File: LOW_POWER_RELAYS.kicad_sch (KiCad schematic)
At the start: 8 parts, among them CN1 6437288-3, U1 YQ506-S-112 DM

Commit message: Modified Relay Page to add Lights, Radiator, and Fuel Pump
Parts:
- removed D2: LED, symbol Device:LED
- removed R1: 10k, symbol Device:R_US
- removed R2: ?, symbol Device:R_US
- added C10: 100n, EasyEDA:CAP-TH_L5.0-W2.5-P5.00-D1.0, symbol Device:C
- added C11, C12, C9: 10u, EasyEDA:CAP-TH_L5.5-W3.8-P5.08-D0.5, symbol Device:C
- added D3, D5: 1N5399, Package_DIP:DIP-40_W15.24mm, symbol Device:D_Zener
- added D6, D7, D8: LED, EasyEDA:LED-TH_BD3.0-P2.54-FD_YELLOW, symbol Device:LED
- added R10, R6, R9: 660, EasyEDA:RES-TH_BD2.4-L6.3-P10.30-D0.6, symbol Device:R_US
- added R5, R7, R8: 10k, EasyEDA:RES-TH_BD2.5-L6.5-P10.50-D0.6, symbol Device:R_US
- added U2, U3: YQ506-S-112 DM, EasyEDA:RELAY-TH_YQ506-S-112DM, symbol EasyEDA:YQ506-S-112DM
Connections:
- net GND: now also C10.2, C11.2, C12.2, C9.2, D3.2 (A), D5.2 (A), R10.2, R5.2, R6.2, R7.2, R8.2, R9.2, U2.86, U3.86
- net PWR_12V: now also C10.1, C11.1, C12.1, C9.1, U2.30, U3.30
- net PWR_EN_FUEL_PUMP: now also D7.2 (A), R7.1
- new net: D8.1 (K), R9.1
- new net: D6.1 (K), R6.1
- new net: D7.1 (K), R10.1
- new net PWR_EN_LIGHTS: D3.1 (K), D8.2 (A), R8.1, U2.85
- new net PWR_EN_RADIATOR: D5.1 (K), D6.2 (A), R5.1, U3.85
- new net PWR_LIGHTS: U2.87
- new net PWR_RADIATOR: U3.87
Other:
- note added: "Author: Brandon Estrada"
- note removed: "We need: 3x THT LEDs, various colors, with THT resistors 1x THT Buzzer, 5V rated"
- moved on the sheet: C7, C8, D1, U1

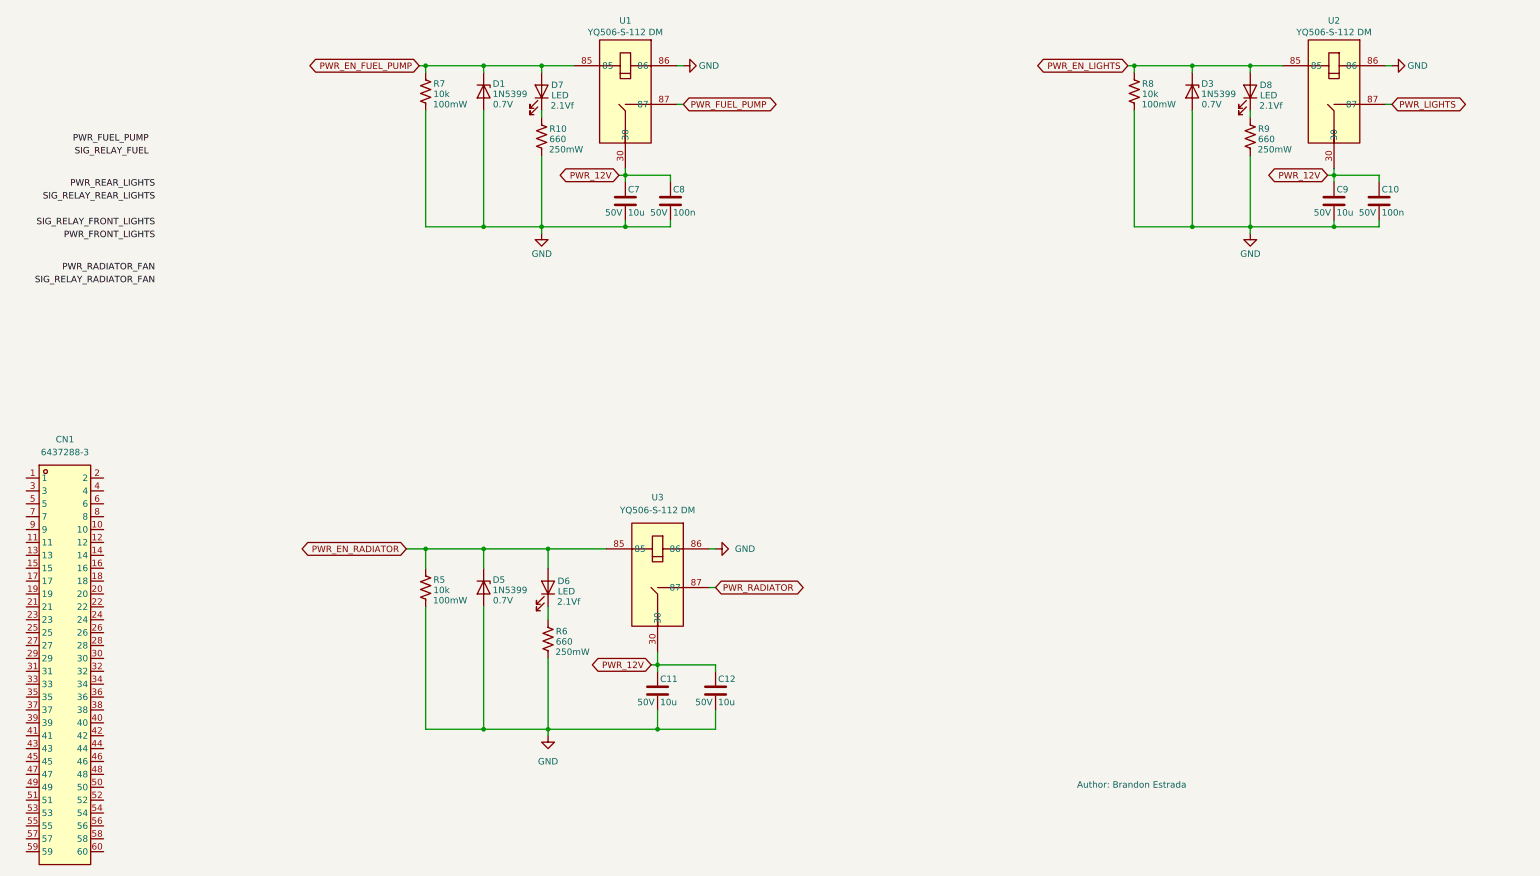
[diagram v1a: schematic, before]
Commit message: Update hub design and add RJ45 connector
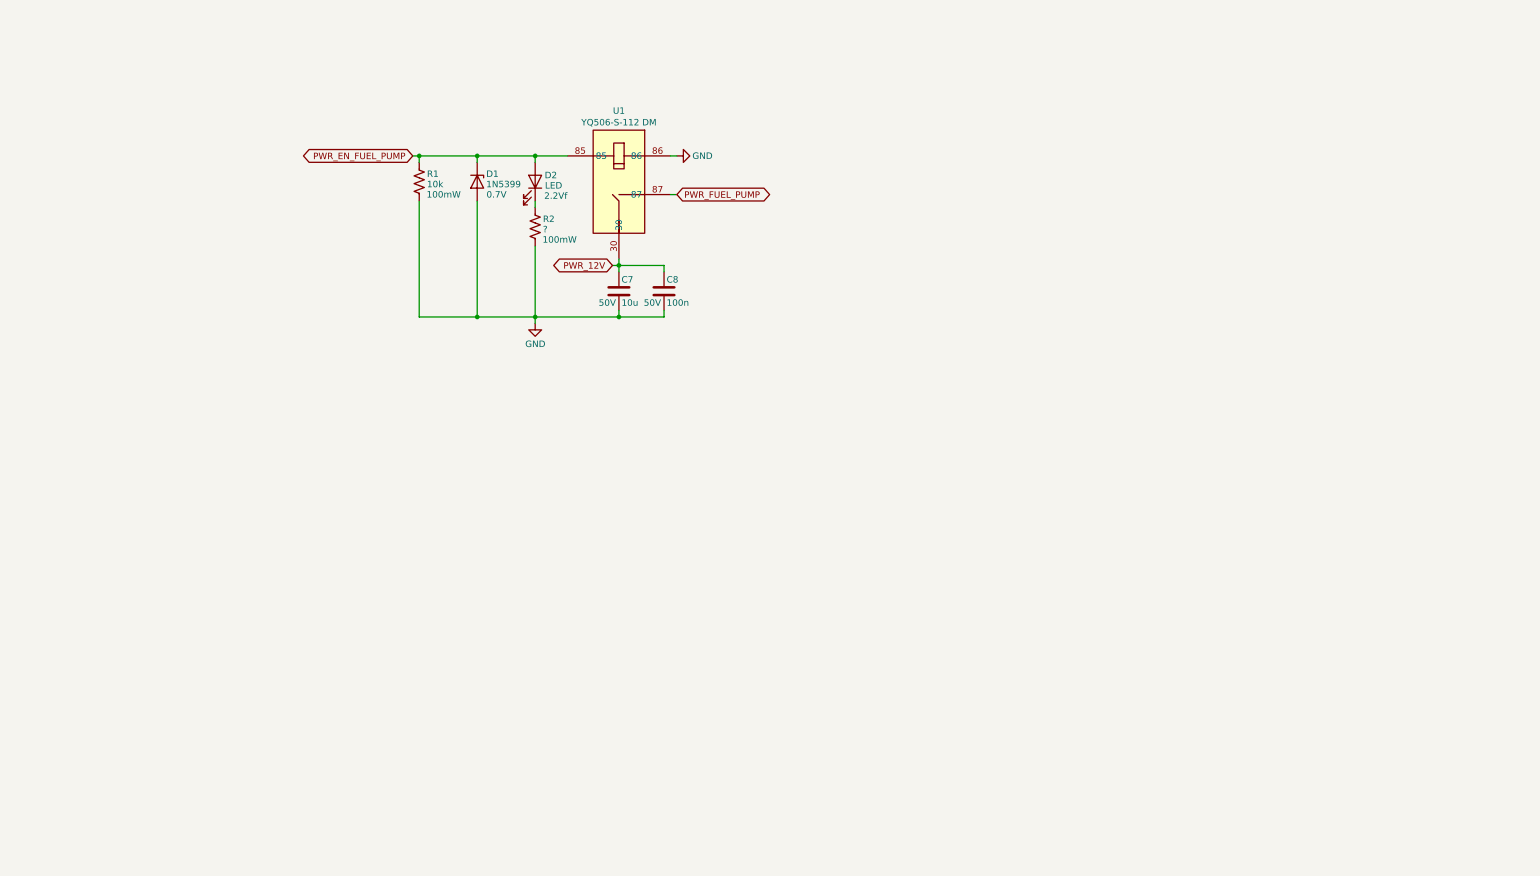
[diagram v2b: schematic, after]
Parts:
- removed C10: 100n, EasyEDA:CAP-TH_L5.0-W2.5-P5.00-D1.0, symbol Device:C
- removed C11, C12, C9: 10u, EasyEDA:CAP-TH_L5.5-W3.8-P5.08-D0.5, symbol Device:C
- removed CN1: 6437288-3, EasyEDA:DSUB-60P_SUPERSEAL, symbol EasyEDA:6437288-3
- removed D3, D5: 1N5399, Package_DIP:DIP-40_W15.24mm, symbol Device:D_Zener
- removed D6, D7, D8: LED, EasyEDA:LED-TH_BD3.0-P2.54-FD_YELLOW, symbol Device:LED
- removed R10, R6, R9: 660, EasyEDA:RES-TH_BD2.4-L6.3-P10.30-D0.6, symbol Device:R_US
- removed R5, R7, R8: 10k, EasyEDA:RES-TH_BD2.5-L6.5-P10.50-D0.6, symbol Device:R_US
- removed U2, U3: YQ506-S-112 DM, EasyEDA:RELAY-TH_YQ506-S-112DM, symbol EasyEDA:YQ506-S-112DM
- added D2: LED, symbol Device:LED
- added R1: 10k, symbol Device:R_US
- added R2: ?, symbol Device:R_US
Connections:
- net GND: now also R1.2, R2.2
- net PWR_EN_FUEL_PUMP: now also D2.2 (A), R1.1
- new net: D2.1 (K), R2.1
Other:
- note removed: "Author: Brandon Estrada"
- moved on the sheet: C7, C8, D1, U1

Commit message: Merge relay and status schematic components
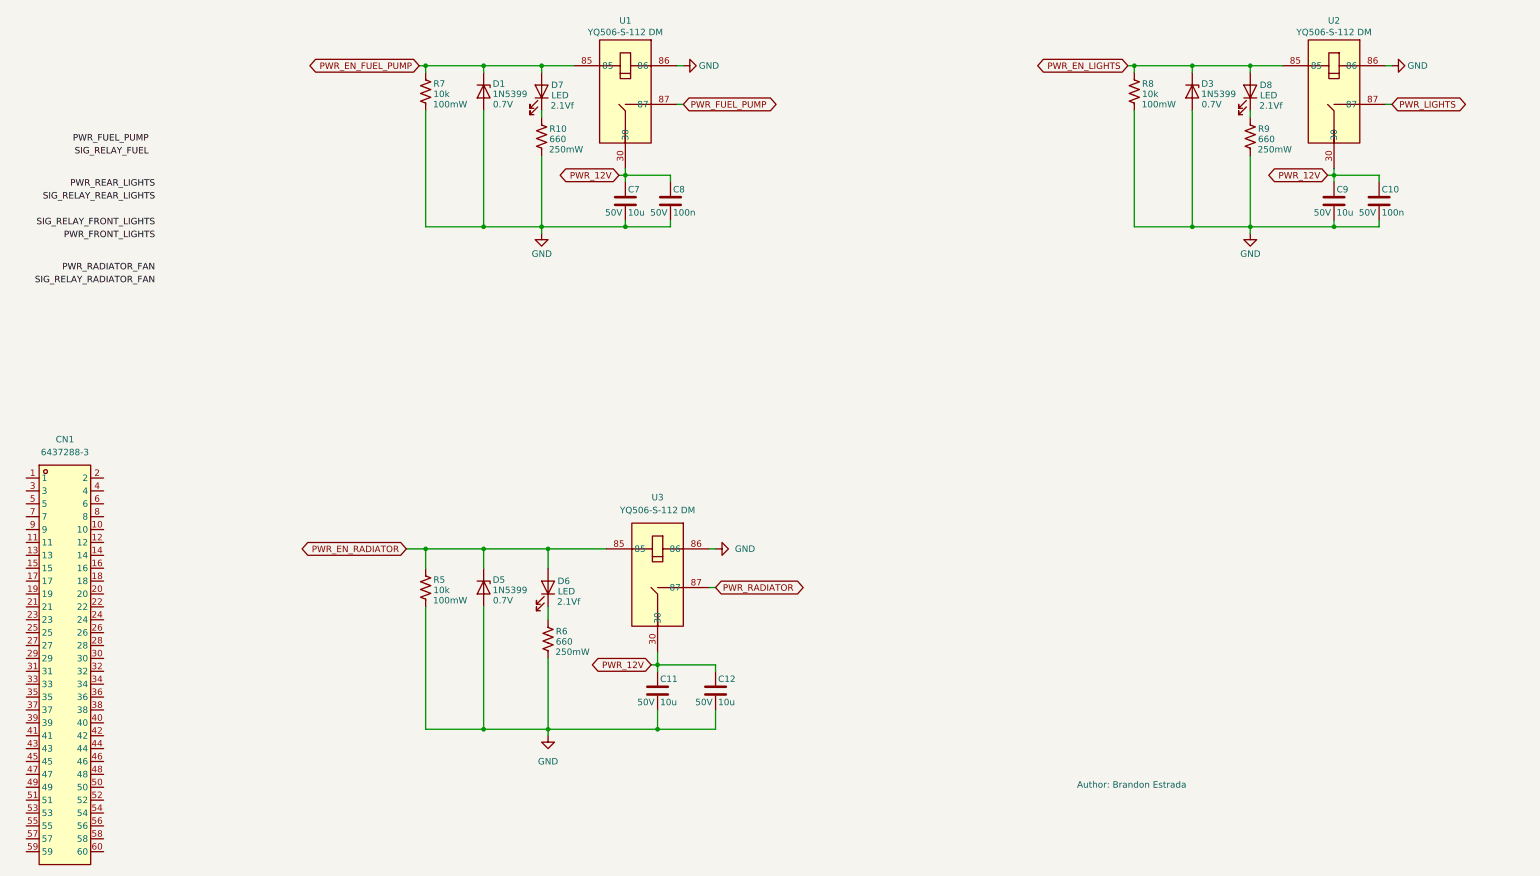
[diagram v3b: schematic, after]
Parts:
- removed D2: LED, symbol Device:LED
- removed R1: 10k, symbol Device:R_US
- removed R2: ?, symbol Device:R_US
- added C10: 100n, EasyEDA:CAP-TH_L5.0-W2.5-P5.00-D1.0, symbol Device:C
- added C11, C12, C9: 10u, EasyEDA:CAP-TH_L5.5-W3.8-P5.08-D0.5, symbol Device:C
- added CN1: 6437288-3, EasyEDA:DSUB-60P_SUPERSEAL, symbol EasyEDA:6437288-3
- added D3, D5: 1N5399, Package_DIP:DIP-40_W15.24mm, symbol Device:D_Zener
- added D6, D7, D8: LED, EasyEDA:LED-TH_BD3.0-P2.54-FD_YELLOW, symbol Device:LED
- added R10, R6, R9: 660, EasyEDA:RES-TH_BD2.4-L6.3-P10.30-D0.6, symbol Device:R_US
- added R5, R7, R8: 10k, EasyEDA:RES-TH_BD2.5-L6.5-P10.50-D0.6, symbol Device:R_US
- added U2, U3: YQ506-S-112 DM, EasyEDA:RELAY-TH_YQ506-S-112DM, symbol EasyEDA:YQ506-S-112DM
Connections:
- net GND: now also C10.2, C11.2, C12.2, C9.2, D3.2 (A), D5.2 (A), R10.2, R5.2, R6.2, R7.2, R8.2, R9.2, U2.86, U3.86
- net PWR_12V: now also C10.1, C11.1, C12.1, C9.1, U2.30, U3.30
- net PWR_EN_FUEL_PUMP: now also D7.2 (A), R7.1
- new net: D8.1 (K), R9.1
- new net: D6.1 (K), R6.1
- new net: D7.1 (K), R10.1
- new net PWR_EN_LIGHTS: D3.1 (K), D8.2 (A), R8.1, U2.85
- new net PWR_EN_RADIATOR: D5.1 (K), D6.2 (A), R5.1, U3.85
- new net PWR_LIGHTS: U2.87
- new net PWR_RADIATOR: U3.87
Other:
- note added: "Author: Brandon Estrada"
- moved on the sheet: C7, C8, D1, U1

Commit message: Cleanup schematics a little bit
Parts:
- removed CN1: 6437288-3, EasyEDA:DSUB-60P_SUPERSEAL, symbol EasyEDA:6437288-3
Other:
- note added: "0"
- note added: "Authors: Isaac Subudhi Brandon Estrada"
- note added: "Mon, Oct, 12, 2026"
- note added: "RAM RACING: HUB V2: Low Power Relays"
- note removed: "Author: Brandon Estrada"
- moved on the sheet: C10, C11, C12, C9, D3, D5, D6, D8, R5, R6, R8, R9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

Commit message: Mapping for M130, cleanup on all sheets, layout start
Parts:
- added C10: 10u, EasyEDA:CAP-TH_L5.5-W3.8-P5.08-D0.5, symbol Device:C
- added C13: 100n, EasyEDA:CAP-TH_L5.0-W2.5-P5.00-D1.0, symbol Device:C
- added D6: 1N5399, Diode_THT:D_DO-15_P10.16mm_Horizontal, symbol Device:D_Zener
- added D9: LED, EasyEDA:LED-TH_BD3.0-P2.54-FD_YELLOW, symbol Device:LED
- added R6: 10k, EasyEDA:RES-TH_BD2.5-L6.5-P10.50-D0.6, symbol Device:R_US
- added R9: 660, EasyEDA:RES-TH_BD2.4-L6.3-P10.30-D0.6, symbol Device:R_US
- added U3: YQ506-S-112 DM, EasyEDA:RELAY-TH_YQ506-S-112DM, symbol EasyEDA:YQ506-S-112DM
- C12: value 10u -> 100n; footprint EasyEDA:CAP-TH_L5.5-W3.8-P5.08-D0.5 -> EasyEDA:CAP-TH_L5.0-W2.5-P5.00-D1.0; LCSC Num (none) -> C254085; LCSC Part C2761740 -> (none)
- D10: renamed from D3; footprint Package_DIP:DIP-40_W15.24mm -> Diode_THT:D_DO-15_P10.16mm_Horizontal
- D4: renamed from D5; footprint Package_DIP:DIP-40_W15.24mm -> Diode_THT:D_DO-15_P10.16mm_Horizontal
- D5: renamed from D1; footprint Package_DIP:DIP-40_W15.24mm -> Diode_THT:D_DO-15_P10.16mm_Horizontal
- renumbered C8 to C11, C9 to C14, C10 to C15, C7 to C8, C11 to C9, D8 to D11, D6 to D7, D7 to D8, R8 to R10, R9 to R11, R5 to R4, R7 to R5, R6 to R7, R10 to R8, U3 to U2, U2 to U4
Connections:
- net GND: now also C10.2, C13.2, D6.2 (A), R6.2, R9.2, U3.86
- net PWR_12V renamed +12V_BATT
- net +12V_BATT: now also C10.1, C13.1, U3.30
- net PWR_EN_FUEL_PUMP renamed EN_HS_FUEL_PUMP
- net PWR_EN_LIGHTS renamed EN_HS_LIGHTS
- net PWR_EN_RADIATOR renamed EN_HS_RADIATOR
- new net: D9.1 (K), R9.1
- new net +12V_MAIN: U3.87
- new net PWR_EN_MAIN: D6.1 (K), D9.2 (A), R6.1, U3.85
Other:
- note added: "Authors: Lead: Isaac Subudhi Main Editor: Brandon Estrada"
- note removed: "Authors: Isaac Subudhi Brandon Estrada"
- moved on the sheet: C11, C14, C15, C8, C9, D10, D11, D4, D5, D7, D8, R10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

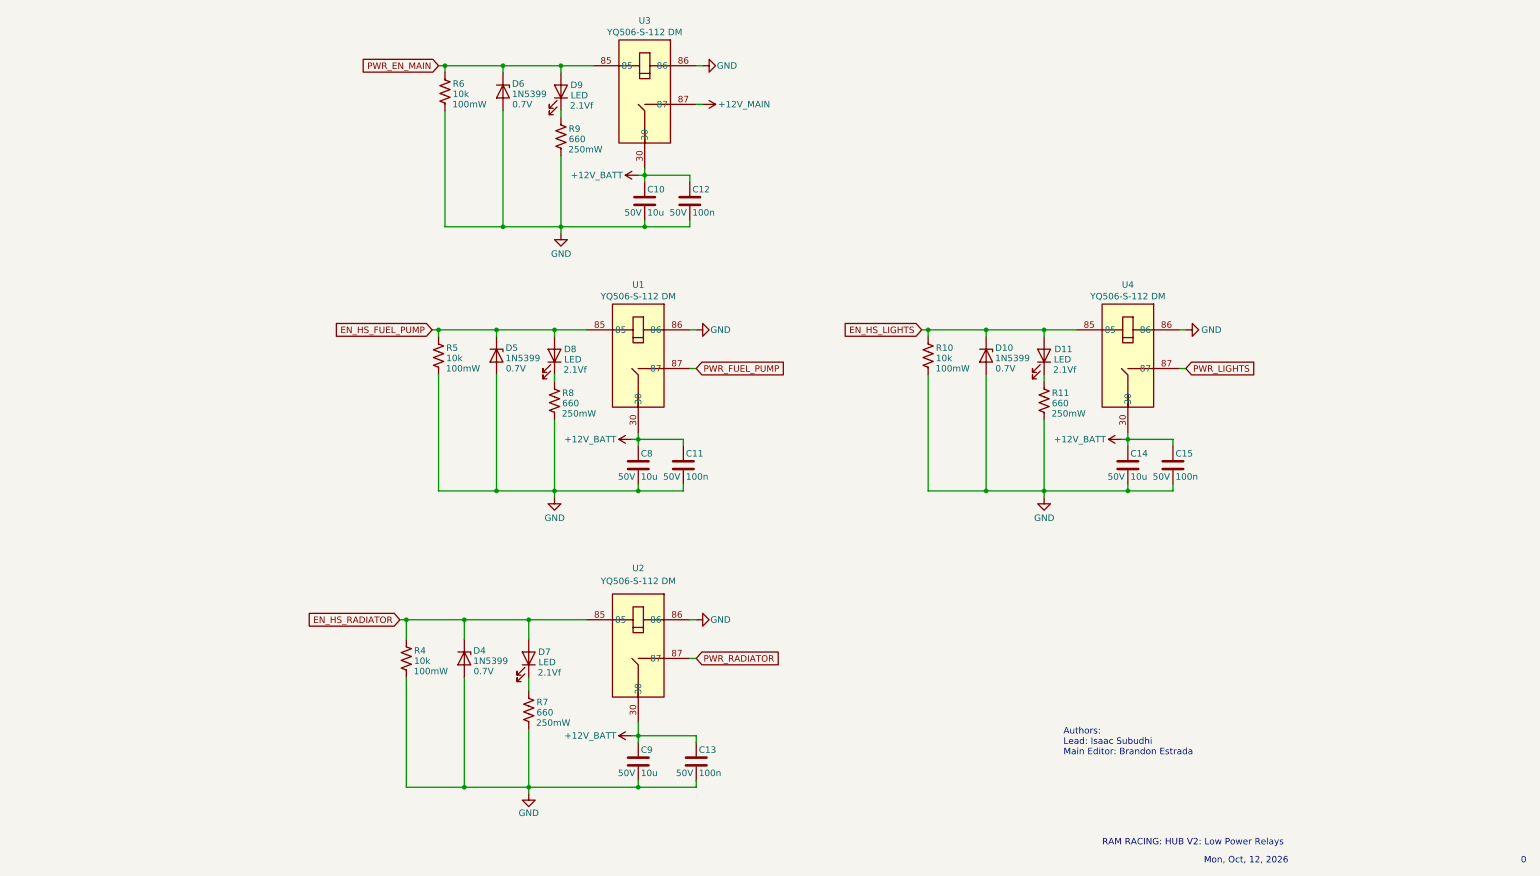
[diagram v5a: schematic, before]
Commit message: Relay layout done, pinout assignments, M1 Notes, and 04 Sch Start
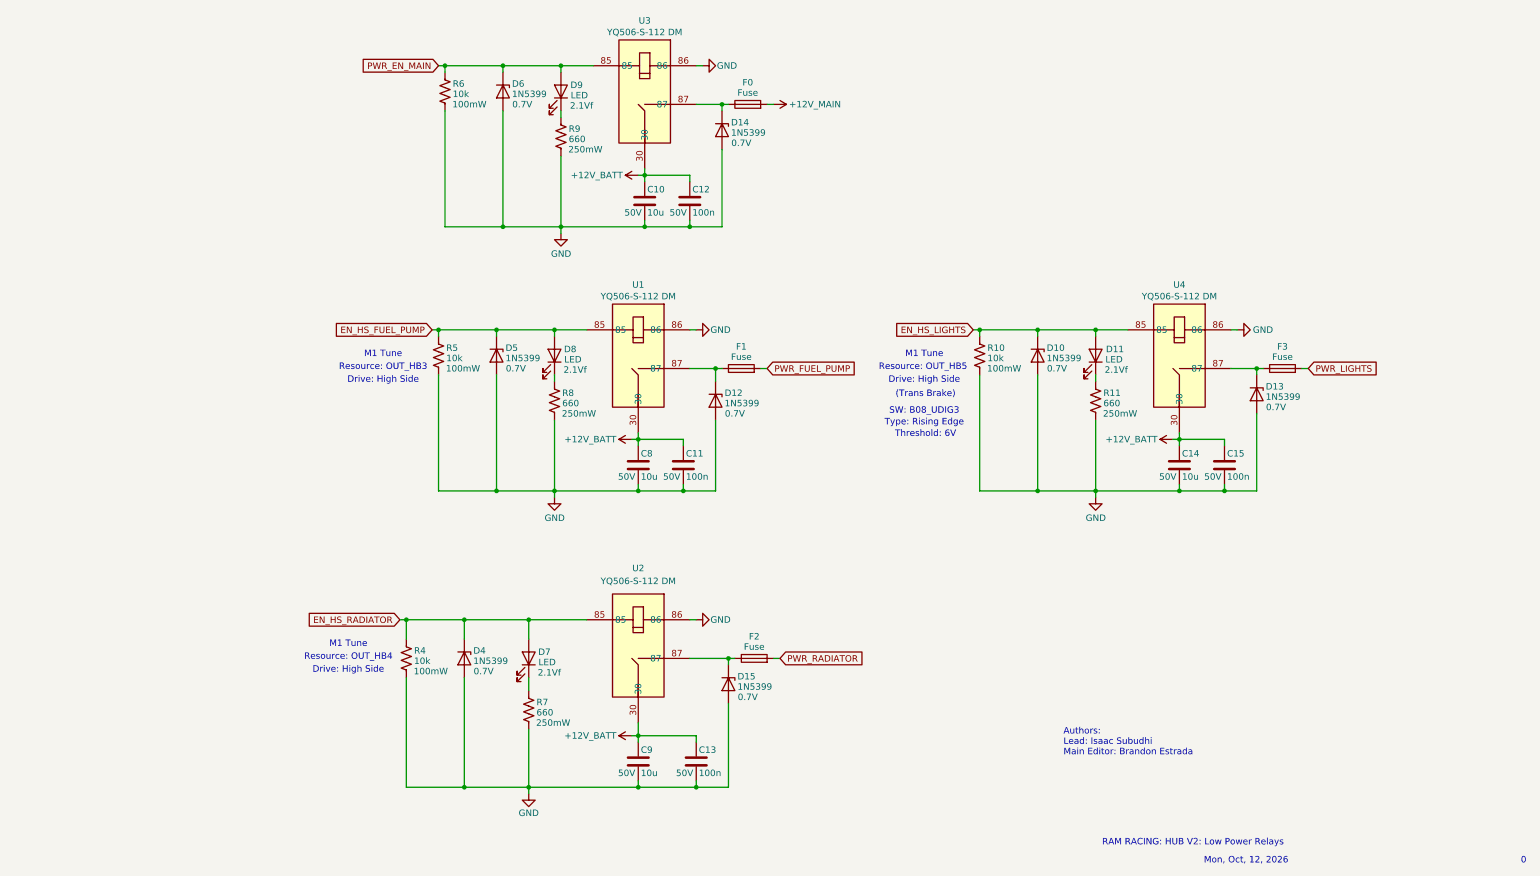
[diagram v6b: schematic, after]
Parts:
- added D12, D13, D14, D15: 1N5399, Diode_THT:D_DO-15_P10.16mm_Horizontal, symbol Device:D_Zener
- added F0, F1, F2, F3: Fuse, EasyEDA:FUSE_3568, symbol Device:Fuse
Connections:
- net +12V_MAIN: now also F0.2; no longer U3.87
- net GND: now also D12.2 (A), D13.2 (A), D14.2 (A), D15.2 (A)
- net PWR_FUEL_PUMP: now also F1.2; no longer U1.87
- net PWR_LIGHTS: now also F3.2; no longer U4.87
- net PWR_RADIATOR: now also F2.2; no longer U2.87
- new net: D13.1 (K), F3.1, U4.87
- new net: D15.1 (K), F2.1, U2.87
- new net: D14.1 (K), F0.1, U3.87
- new net: D12.1 (K), F1.1, U1.87
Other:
- note added: "(Trans Brake)"
- note added: "Drive: High Side"
- note added: "M1 Tune"
- note added: "Resource: OUT_HB3"
- note added: "Resource: OUT_HB4"
- note added: "Resource: OUT_HB5"
- note added: "SW: B08_UDIG3"
- note added: "Threshold: 6V"
- note added: "Type: Rising Edge"
- moved on the sheet: C14, C15, D10, D11, R10, R11, U4

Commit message: High current layout work & Simulation
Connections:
- net PWR_LIGHTS_BEFORE_FUSE: now reaches D13.1 (K), F3.1, U4.87
- net PWR_RADIATOR_BEFORE_FUSE: now reaches D15.1 (K), F2.1, U2.87
- net PWR_MAIN_BEFORE_FUSE: now reaches D14.1 (K), F0.1, U3.87
- net PWR_FUEL_PUMP_BEFORE_FUSE: now reaches D12.1 (K), F1.1, U1.87
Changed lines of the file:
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@@
+		)
+	)
+	(label "PWR_LIGHTS_BEFORE_FUSE"
+		(at 215.9 96.52 180)
+		(effects
+			(font
+				(size 0.254 0.254)
+			)
+			(justify right bottom)
+		)
+	)
+	(label "PWR_RADIATOR_BEFORE_FUSE"
+		(at 111.76 153.67 180)
+		(effects
+			(font
+				(size 0.254 0.254)
+			)
+			(justify right bottom)
+		)
+	)
+	(label "PWR_FUEL_PUMP_BEFORE_FUSE"
+		(at 109.22 96.52 180)
+		(effects
+			(font
+				(size 0.254 0.254)
+			)
+			(justify right bottom)
+		)
+	)
+	(label "PWR_MAIN_BEFORE_FUSE"
+		(at 110.49 44.45 180)
+		(effects
+			(font
+				(size 0.254 0.254)
+			)
+			(justify right bottom)
 		)
 	)
